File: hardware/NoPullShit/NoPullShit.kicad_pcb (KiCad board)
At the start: 2 copper layers, 35 x 35 mm, 52 parts, among them J1 USB Power, J2 Load cell, J3 Batt+, J4 Batt-, J5 ICSP, J6 UART, J7 Spk+, J8 Spk-, Q1 BC808, Q2 BC817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

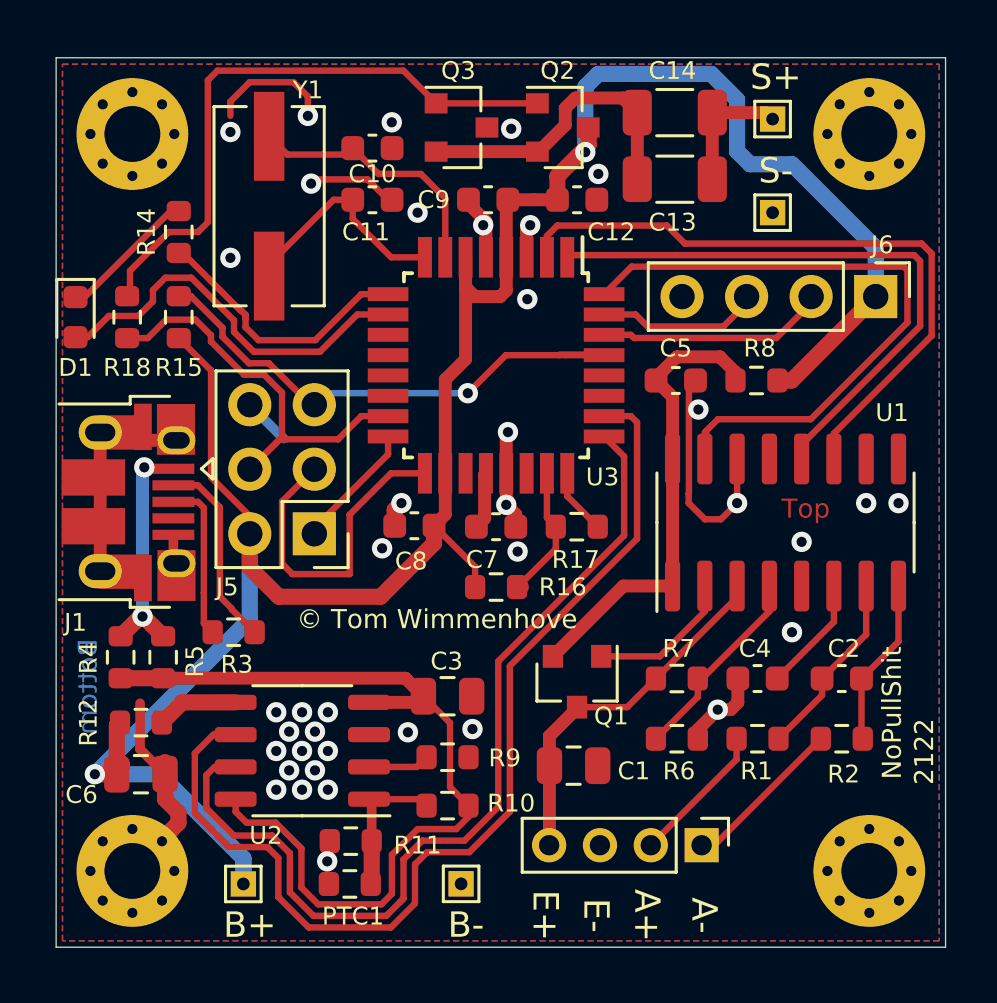
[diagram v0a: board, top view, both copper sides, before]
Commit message: PSU current sense fix + some shuffling
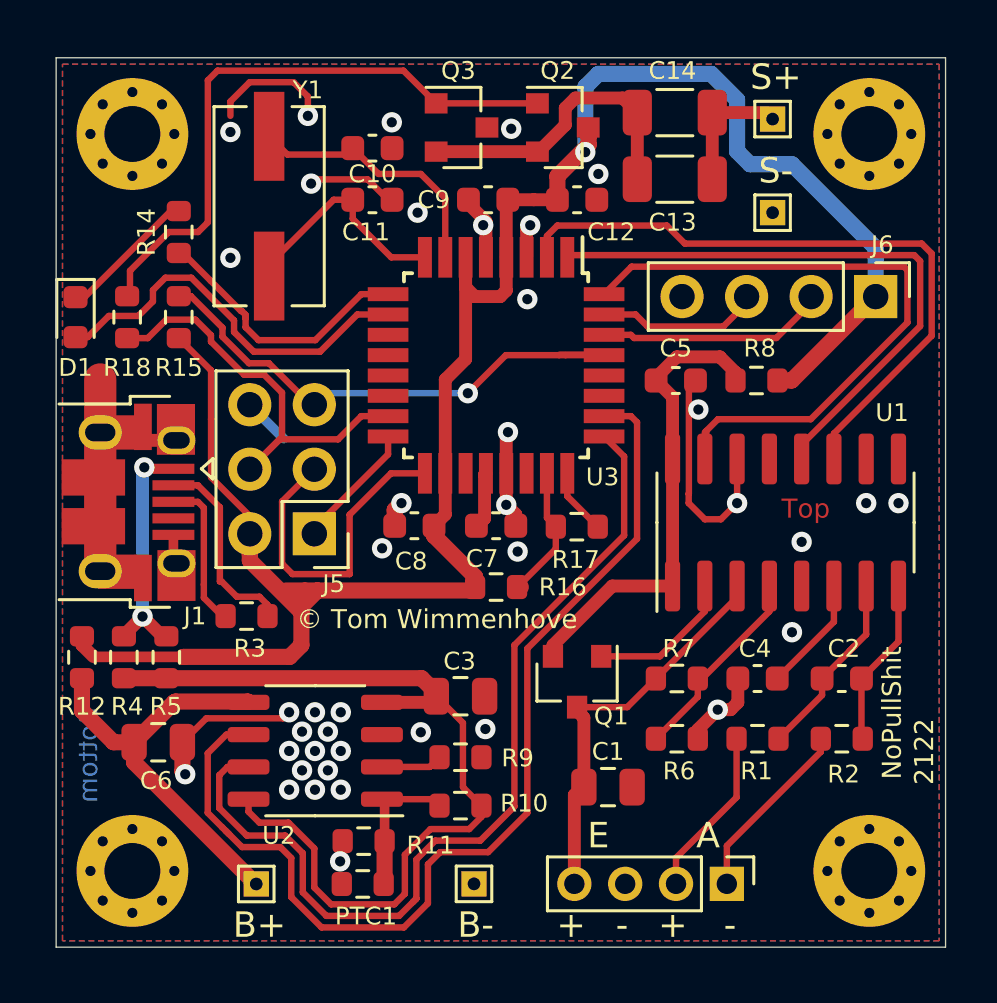
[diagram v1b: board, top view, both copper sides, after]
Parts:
- moved R12 3.46 mm to (26.4, 54.0), turned to 90 degrees
- moved J2 1.82 mm to (51.8, 62.9)
- moved C1 1.60 mm to (47.1, 59.1)
- moved C6 1.43 mm to (29.4, 57.3)
- moved R3 0.81 mm to (32.9, 52.4)
- moved C3 0.51 mm to (41.3, 55.5)
- moved J3 0.51 mm to (33.3, 62.9)
- moved J4 0.51 mm to (41.8, 62.9)
- moved PTC1 0.51 mm to (37.5, 62.9)
- moved R10 0.51 mm to (41.3, 59.8)
- moved R9 0.51 mm to (41.3, 57.9)
- moved R11 0.51 mm to (37.5, 61.2)
- moved U2 0.51 mm to (35.6, 57.7)
- moved R4 0.13 mm to (28.1, 54.0)
- moved R5 0.13 mm to (29.7, 54.0)
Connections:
- C6 pad 1: VCC -> Net-(C6-Pad1)
- J3 pad 1: VCC -> Net-(C6-Pad1)
- R12 pad 1: Net-(R12-Pad1) -> Net-(C6-Pad1)
- U2 pad 5: Net-(R12-Pad1) -> Net-(C6-Pad1)
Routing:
- net Net-(C6-Pad1): track 0.00 -> 16.6 mm
- net VCC: track 95.3 -> 85.3 mm, vias 2 -> 1
- net GND: track 53.6 -> 58.7 mm, vias 39 -> 40
- net Net-(R12-Pad1): track 3.23 -> 0.00 mm
- net Net-(C1-Pad1): track 14.5 -> 15.9 mm
- net Net-(J2-Pad2): track 5.59 -> 6.70 mm
- net Net-(J2-Pad1): track 6.43 -> 7.24 mm
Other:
- board text added: "+"
- board text added: "-"
- board text added: "A"
- board text added: "E"
- board text removed: "A+"
- board text removed: "A-"
- board text removed: "E+"
- board text removed: "E-"

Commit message: Better ground around x-tal
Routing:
- net GND: vias 40 -> 47

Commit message: Slightly improved ground-plane
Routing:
- net /RATE: track 26.3 -> 20.2 mm
- net GND: track 58.7 -> 53.8 mm, vias 47 -> 40
- net /SCK: track 26.3 -> 25.2 mm
- net Net-(Q2-Pad1): track 24.2 -> 23.2 mm
- net /DOUT: track 23.7 -> 22.8 mm
- net VCC: track 85.3 -> 85.9 mm
- net Net-(J1-Pad2): track 7.80 -> 7.24 mm
- net Net-(C6-Pad1): track 16.6 -> 17.1 mm

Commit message: Hopefully ready for JLCPCB
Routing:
- net GND: track 53.8 -> 57.0 mm
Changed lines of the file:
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@@
-(kicad_pcb (version 20171130) (host pcbnew 5.1.10-88a1d61d58~88~ubuntu20.10.1)
+(kicad_pcb (version 20171130) (host pcbnew 5.1.10-88a1d61d58~88~ubuntu18.04.1)
   (general
     (thickness 0.8)
     (drawings 20)
-    (tracks 455)
+    (tracks 458)
     (zones 0)
     (modules 52)
@@
   )
   (setup
-    (last_trace_width 0.254)
+    (last_trace_width 0.508)
     (user_trace_width 0.254)
     (user_trace_width 0.381)
@@
     (visible_elements FFFFFF7F)
     (pcbplotparams
-      (layerselection 0x01000_7fffffff)
-      (usegerberextensions false)
-      (usegerberattributes true)
-      (usegerberadvancedattributes true)
-      (creategerberjobfile true)
+      (layerselection 0x010fc_ffffffff)
+      (usegerberextensions true)
+      (usegerberattributes false)
+      (usegerberadvancedattributes false)
+      (creategerberjobfile false)
       (excludeedgelayer true)
-      (linewidth 0.100000)
+      (linewidth 0.150000)
       (plotframeref false)
       (viasonmask false)
@@
       (psa4output false)
       (plotreference true)
-      (plotvalue true)
+      (plotvalue false)
       (plotinvisibletext false)
       (padsonsilk false)
-      (subtractmaskfromsilk false)
-      (outputformat 4)
+      (subtractmaskfromsilk true)
+      (outputformat 1)
       (mirror false)
       (drillshape 0)
@@
   (segment (start 27.135 50.605) (end 27.135 43.057) (width 1.27) (layer F.Cu) (net 1))
   (via (at 35.306 38.528) (size 0.8) (drill 0.4) (layers F.Cu B.Cu) (net 1))
+  (segment (start 54.356 53.006) (end 53.494 53.006) (width 0.508) (layer F.Cu) (net 1))
+  (segment (start 52.226 54.274) (end 52.226 54.828) (width 0.508) (layer F.Cu) (net 1))
+  (segment (start 53.494 53.006) (end 52.226 54.274) (width 0.508) (layer F.Cu) (net 1))
   (segment (start 49.077347 54.828) (end 49.001 54.828) (width 0.254) (layer F.Cu) (net 2))
   (segment (start 47.874 55.955) (end 49.001 54.828) (width 0.254) (layer F.Cu) (net 2))
